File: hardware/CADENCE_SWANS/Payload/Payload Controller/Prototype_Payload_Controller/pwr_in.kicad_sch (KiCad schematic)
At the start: 0 parts

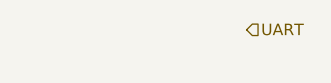
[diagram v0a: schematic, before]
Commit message: Instrument.sch updates
Added Control Readout module, and made it more legible and clean
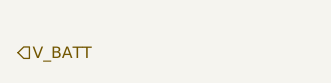
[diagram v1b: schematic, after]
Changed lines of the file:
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@@
 	(generator_version "9.0")
 	(paper "A5")
-	(hierarchical_label "UART"
+	(hierarchical_label "V_BATT"
 		(shape input)
-		(at 85.09 54.61 0)
+		(at 59.69 57.15 0)
 		(effects
 			(font

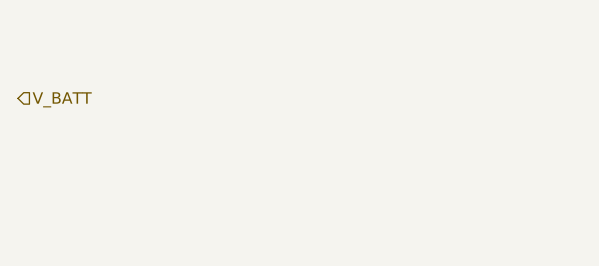
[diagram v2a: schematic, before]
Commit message: power management updates
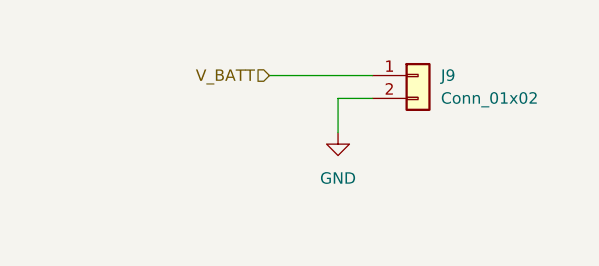
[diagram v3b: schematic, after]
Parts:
- added J9: Conn_01x02, symbol Connector_Generic:Conn_01x02
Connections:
- net V_BATT: now also J9.1 (Pin_1)
- new net GND: J9.2 (Pin_2)
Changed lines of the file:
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@@
 	(generator_version "9.0")
 	(paper "A5")
+	(wire
+		(pts
+			(xy 95.25 57.15) (xy 99.06 57.15)
+		)
+		(stroke
+			(width 0)
+			(type default)
+		)
+	)
+	(wire
+		(pts
+			(xy 95.25 60.96) (xy 95.25 57.15)
+		)
+		(stroke
+			(width 0)
+			(type default)
+		)
+	)
+	(wire
+		(pts
+			(xy 87.63 54.61) (xy 99.06 54.61)
+		)
+		(stroke
+			(width 0)
+			(type default)
+		)
+	)
 	(hierarchical_label "V_BATT"
 		(shape input)
-		(at 59.69 57.15 0)
+		(at 87.63 54.61 180)
 		(effects
 			(font
 				(size 1.27 1.27)
 			)
-			(justify left)
+			(justify right)
 		)
 	)
+	(symbol
+		(lib_id "power:GND")
+		(at 95.25 60.96 0)
+		(unit 1)
+		(exclude_from_sim no)
+		(in_bom yes)
+		(on_board yes)
+		(dnp no)
+		(fields_autoplaced yes)
+		(property "Reference" "#PWR024"
+			(at 95.25 67.31 0)
+			(effects
+				(font
+					(size 1.27 1.27)
+				)
+				(hide yes)
+			)
+		)
+		(property "Value" "GND"
+			(at 95.25 66.04 0)
+			(effects
+				(font
+					(size 1.27 1.27)
+				)
+			)
+		)
+		(property "Footprint" ""
+			(at 95.25 60.96 0)
+			(effects
+				(font
+					(size 1.27 1.27)
+				)
+				(hide yes)
+			)
+		)
+		(property "Datasheet" ""
+			(at 95.25 60.96 0)
+			(effects
+				(font
+					(size 1.27 1.27)
+				)
+				(hide yes)
+			)
+		)
+		(property "Description" "Power symbol creates a global label with name \"GND\" , ground"
+			(at 95.25 60.96 0)
+			(effects
+				(font
+					(size 1.27 1.27)
+				)
+				(hide yes)
+			)
+		)
+		(pin "1"
+		)
+		(instances
+			(project ""
+				(path "/866a965d-c307-40b7-9977-69e77fc0dc82/4cf906e6-065c-4b10-a5a2-987a95214f7a"
+					(reference "#PWR024")
+					(unit 1)
+				)
+			)
+		)
+	)
+	(symbol
+		(lib_id "Connector_Generic:Conn_01x02")
+		(at 104.14 54.61 0)
+		(unit 1)
+		(exclude_from_sim no)
+		(in_bom yes)
+		(on_board yes)
+		(dnp no)
+		(fields_autoplaced yes)
+		(property "Reference" "J9"
+			(at 106.68 54.6099 0)
+			(effects
+				(font
+					(size 1.27 1.27)
+				)
+				(justify left)
+			)
+		)
+		(property "Value" "Conn_01x02"
+			(at 106.68 57.1499 0)
+			(effects
+				(font
+					(size 1.27 1.27)
+				)
+				(justify left)
+			)
+		)
+		(property "Footprint" ""
+			(at 104.14 54.61 0)
+			(effects
+				(font
+					(size 1.27 1.27)
+				)
+				(hide yes)
+			)
+		)
+		(property "Datasheet" "~"
+			(at 104.14 54.61 0)
+			(effects
+				(font
+					(size 1.27 1.27)
+				)
+				(hide yes)
+			)
+		)
+		(property "Description" "Generic connector, single row, 01x02, script generated (kicad-library-utils/schlib/autogen/connector/)"
+			(at 104.14 54.61 0)
+			(effects
+				(font
+					(size 1.27 1.27)
+				)
+				(hide yes)
+			)
+		)
+		(pin "1"
+		)
+		(pin "2"
+		)
+		(instances
+			(project ""
+				(path "/866a965d-c307-40b7-9977-69e77fc0dc82/4cf906e6-065c-4b10-a5a2-987a95214f7a"
+					(reference "J9")
+					(unit 1)
+				)
+			)
+		)
+	)

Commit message: updates
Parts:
- J9: footprint (none) -> Connector_AMASS:AMASS_XT60-F_1x02_P7.20mm_Vertical
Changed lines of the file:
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@@
 	(generator_version "9.0")
 	(paper "A5")
+	(junction
+		(at 92.71 54.61)
+		(diameter 0)
+		(color 0 0 0 0)
+	)
+	(wire
+		(pts
+			(xy 92.71 54.61) (xy 99.06 54.61)
+		)
+		(stroke
+			(width 0)
+			(type default)
+		)
+	)
 	(wire
 		(pts
@@
 	(wire
 		(pts
-			(xy 87.63 54.61) (xy 99.06 54.61)
+			(xy 87.63 54.61) (xy 92.71 54.61)
 		)
 		(stroke
@@
 	)
 	(symbol
+		(lib_id "power:PWR_FLAG")
+		(at 92.71 54.61 0)
+		(unit 1)
+		(exclude_from_sim no)
+		(in_bom yes)
+		(on_board yes)
+		(dnp no)
+		(fields_autoplaced yes)
+		(property "Reference" "#FLG08"
+			(at 92.71 52.705 0)
+			(effects
+				(font
+					(size 1.27 1.27)
+				)
+				(hide yes)
+			)
+		)
+		(property "Value" "PWR_FLAG"
+			(at 92.71 49.53 0)
+			(effects
+				(font
+					(size 1.27 1.27)
+				)
+			)
+		)
+		(property "Footprint" ""
+			(at 92.71 54.61 0)
+			(effects
+				(font
+					(size 1.27 1.27)
+				)
+				(hide yes)
+			)
+		)
+		(property "Datasheet" "~"
+			(at 92.71 54.61 0)
+			(effects
+				(font
+					(size 1.27 1.27)
+				)
+				(hide yes)
+			)
+		)
+		(property "Description" "Special symbol for telling ERC where power comes from"
+			(at 92.71 54.61 0)
+			(effects
+				(font
+					(size 1.27 1.27)
+				)
+				(hide yes)
+			)
+		)
+		(pin "1"
+		)
+		(instances
+			(project "Payload_Controller_EM"
+				(path "/866a965d-c307-40b7-9977-69e77fc0dc82/4cf906e6-065c-4b10-a5a2-987a95214f7a"
+					(reference "#FLG08")
+					(unit 1)
+				)
+			)
+		)
+	)
+	(symbol
 		(lib_id "Connector_Generic:Conn_01x02")
 		(at 104.14 54.61 0)
@@
 			)
 		)
-		(property "Footprint" ""
+		(property "Footprint" "Connector_AMASS:AMASS_XT60-F_1x02_P7.20mm_Vertical"
 			(at 104.14 54.61 0)
 			(effects

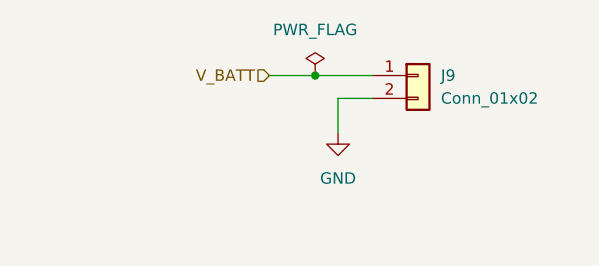
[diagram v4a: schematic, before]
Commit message: linked more footprints
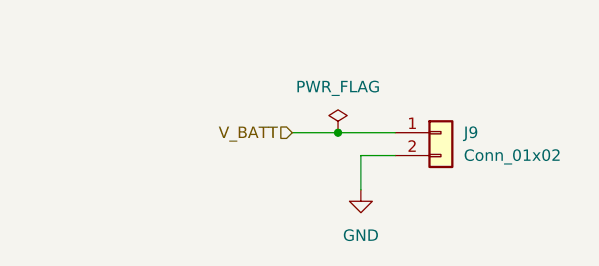
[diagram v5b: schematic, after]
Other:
- moved on the sheet: J9
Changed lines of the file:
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@@
 	(paper "A5")
 	(junction
-		(at 92.71 54.61)
+		(at 95.25 60.96)
 		(diameter 0)
 		(color 0 0 0 0)
@@
 	(wire
 		(pts
-			(xy 92.71 54.61) (xy 99.06 54.61)
-		)
-		(stroke
-			(width 0)
-			(type default)
-		)
-	)
-	(wire
-		(pts
-			(xy 95.25 57.15) (xy 99.06 57.15)
-		)
-		(stroke
-			(width 0)
-			(type default)
-		)
-	)
-	(wire
-		(pts
-			(xy 95.25 60.96) (xy 95.25 57.15)
-		)
-		(stroke
-			(width 0)
-			(type default)
-		)
-	)
-	(wire
-		(pts
-			(xy 87.63 54.61) (xy 92.71 54.61)
+			(xy 95.25 60.96) (xy 101.6 60.96)
+		)
+		(stroke
+			(width 0)
+			(type default)
+		)
+	)
+	(wire
+		(pts
+			(xy 97.79 63.5) (xy 101.6 63.5)
+		)
+		(stroke
+			(width 0)
+			(type default)
+		)
+	)
+	(wire
+		(pts
+			(xy 97.79 67.31) (xy 97.79 63.5)
+		)
+		(stroke
+			(width 0)
+			(type default)
+		)
+	)
+	(wire
+		(pts
+			(xy 90.17 60.96) (xy 95.25 60.96)
 		)
 		(stroke
@@
 	(hierarchical_label "V_BATT"
 		(shape input)
-		(at 87.63 54.61 180)
+		(at 90.17 60.96 180)
 		(effects
 			(font
@@
 	(symbol
 		(lib_id "power:GND")
+		(at 97.79 67.31 0)
+		(unit 1)
+		(exclude_from_sim no)
+		(in_bom yes)
+		(on_board yes)
+		(dnp no)
+		(fields_autoplaced yes)
+		(property "Reference" "#PWR024"
+			(at 97.79 73.66 0)
+			(effects
+				(font
+					(size 1.27 1.27)
+				)
+				(hide yes)
+			)
+		)
+		(property "Value" "GND"
+			(at 97.79 72.39 0)
+			(effects
+				(font
+					(size 1.27 1.27)
+				)
+			)
+		)
+		(property "Footprint" ""
+			(at 97.79 67.31 0)
+			(effects
+				(font
+					(size 1.27 1.27)
+				)
+				(hide yes)
+			)
+		)
+		(property "Datasheet" ""
+			(at 97.79 67.31 0)
+			(effects
+				(font
+					(size 1.27 1.27)
+				)
+				(hide yes)
+			)
+		)
+		(property "Description" "Power symbol creates a global label with name \"GND\" , ground"
+			(at 97.79 67.31 0)
+			(effects
+				(font
+					(size 1.27 1.27)
+				)
+				(hide yes)
+			)
+		)
+		(pin "1"
+		)
+		(instances
+			(project ""
+				(path "/866a965d-c307-40b7-9977-69e77fc0dc82/4cf906e6-065c-4b10-a5a2-987a95214f7a"
+					(reference "#PWR024")
+					(unit 1)
+				)
+			)
+		)
+	)
+	(symbol
+		(lib_id "power:PWR_FLAG")
 		(at 95.25 60.96 0)
 		(unit 1)
@@
 		(dnp no)
 		(fields_autoplaced yes)
-		(property "Reference" "#PWR024"
-			(at 95.25 67.31 0)
-			(effects
-				(font
-					(size 1.27 1.27)
-				)
-				(hide yes)
-			)
-		)
-		(property "Value" "GND"
-			(at 95.25 66.04 0)
+		(property "Reference" "#FLG08"
+			(at 95.25 59.055 0)
+			(effects
+				(font
+					(size 1.27 1.27)
+				)
+				(hide yes)
+			)
+		)
+		(property "Value" "PWR_FLAG"
+			(at 95.25 55.88 0)
 			(effects
 				(font
@@
 			)
 		)
-		(property "Datasheet" ""
+		(property "Datasheet" "~"
 			(at 95.25 60.96 0)
 			(effects
@@
 			)
 		)
-		(property "Description" "Power symbol creates a global label with name \"GND\" , ground"
+		(property "Description" "Special symbol for telling ERC where power comes from"
 			(at 95.25 60.96 0)
-			(effects
-				(font
-					(size 1.27 1.27)
-				)
-				(hide yes)
-			)
-		)
-		(pin "1"
-		)
-		(instances
-			(project ""
-				(path "/866a965d-c307-40b7-9977-69e77fc0dc82/4cf906e6-065c-4b10-a5a2-987a95214f7a"
-					(reference "#PWR024")
-					(unit 1)
-				)
-			)
-		)
-	)
-	(symbol
-		(lib_id "power:PWR_FLAG")
-		(at 92.71 54.61 0)
-		(unit 1)
-		(exclude_from_sim no)
-		(in_bom yes)
-		(on_board yes)
-		(dnp no)
-		(fields_autoplaced yes)
-		(property "Reference" "#FLG08"
-			(at 92.71 52.705 0)
-			(effects
-				(font
-					(size 1.27 1.27)
-				)
-				(hide yes)
-			)
-		)
-		(property "Value" "PWR_FLAG"
-			(at 92.71 49.53 0)
-			(effects
-				(font
-					(size 1.27 1.27)
-				)
-			)
-		)
-		(property "Footprint" ""
-			(at 92.71 54.61 0)
-			(effects
-				(font
-					(size 1.27 1.27)
-				)
-				(hide yes)
-			)
-		)
-		(property "Datasheet" "~"
-			(at 92.71 54.61 0)
-			(effects
-				(font
-					(size 1.27 1.27)
-				)
-				(hide yes)
-			)
-		)
-		(property "Description" "Special symbol for telling ERC where power comes from"
-			(at 92.71 54.61 0)
 			(effects
 				(font
@@
 	(symbol
 		(lib_id "Connector_Generic:Conn_01x02")
-		(at 104.14 54.61 0)
+		(at 106.68 60.96 0)
 		(unit 1)
 		(exclude_from_sim no)
@@
 		(fields_autoplaced yes)
 		(property "Reference" "J9"
-			(at 106.68 54.6099 0)
+			(at 109.22 60.9599 0)
 			(effects
 				(font
@@
 		)
 		(property "Value" "Conn_01x02"
-			(at 106.68 57.1499 0)
+			(at 109.22 63.4999 0)
 			(effects
 				(font
@@
 		)
 		(property "Footprint" "Connector_AMASS:AMASS_XT60-F_1x02_P7.20mm_Vertical"
-			(at 104.14 54.61 0)
+			(at 106.68 60.96 0)
 			(effects
 				(font
@@
 		)
 		(property "Datasheet" "~"
-			(at 104.14 54.61 0)
+			(at 106.68 60.96 0)
 			(effects
 				(font
@@
 		)
 		(property "Description" "Generic connector, single row, 01x02, script generated (kicad-library-utils/schlib/autogen/connector/)"
-			(at 104.14 54.61 0)
-			(effects
-				(font
+			(at 106.68 60.96 0)
+			(effects
+				(font

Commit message: updates
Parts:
- renumbered J9 to J14
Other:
- moved on the sheet: J14
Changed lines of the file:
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@@
 	(paper "A5")
 	(junction
-		(at 95.25 60.96)
+		(at 91.44 57.15)
 		(diameter 0)
 		(color 0 0 0 0)
@@
 	(wire
 		(pts
-			(xy 95.25 60.96) (xy 101.6 60.96)
-		)
-		(stroke
-			(width 0)
-			(type default)
-		)
-	)
-	(wire
-		(pts
-			(xy 97.79 63.5) (xy 101.6 63.5)
-		)
-		(stroke
-			(width 0)
-			(type default)
-		)
-	)
-	(wire
-		(pts
-			(xy 97.79 67.31) (xy 97.79 63.5)
-		)
-		(stroke
-			(width 0)
-			(type default)
-		)
-	)
-	(wire
-		(pts
-			(xy 90.17 60.96) (xy 95.25 60.96)
+			(xy 91.44 57.15) (xy 85.09 57.15)
+		)
+		(stroke
+			(width 0)
+			(type default)
+		)
+	)
+	(wire
+		(pts
+			(xy 88.9 59.69) (xy 85.09 59.69)
+		)
+		(stroke
+			(width 0)
+			(type default)
+		)
+	)
+	(wire
+		(pts
+			(xy 88.9 63.5) (xy 88.9 59.69)
+		)
+		(stroke
+			(width 0)
+			(type default)
+		)
+	)
+	(wire
+		(pts
+			(xy 96.52 57.15) (xy 91.44 57.15)
 		)
 		(stroke
@@
 	(hierarchical_label "V_BATT"
 		(shape input)
-		(at 90.17 60.96 180)
+		(at 96.52 57.15 0)
 		(effects
 			(font
 				(size 1.27 1.27)
 			)
-			(justify right)
+			(justify left)
 		)
 	)
 	(symbol
 		(lib_id "power:GND")
-		(at 97.79 67.31 0)
+		(at 88.9 63.5 0)
+		(mirror y)
 		(unit 1)
 		(exclude_from_sim no)
@@
 		(dnp no)
 		(fields_autoplaced yes)
-		(property "Reference" "#PWR024"
-			(at 97.79 73.66 0)
+		(property "Reference" "#PWR0102"
+			(at 88.9 69.85 0)
 			(effects
 				(font
@@
 		)
 		(property "Value" "GND"
-			(at 97.79 72.39 0)
+			(at 88.9 68.58 0)
 			(effects
 				(font
@@
 		)
 		(property "Footprint" ""
-			(at 97.79 67.31 0)
+			(at 88.9 63.5 0)
 			(effects
 				(font
@@
 		)
 		(property "Datasheet" ""
-			(at 97.79 67.31 0)
+			(at 88.9 63.5 0)
 			(effects
 				(font
@@
 		)
 		(property "Description" "Power symbol creates a global label with name \"GND\" , ground"
-			(at 97.79 67.31 0)
+			(at 88.9 63.5 0)
 			(effects
 				(font
@@
 			(project ""
 				(path "/866a965d-c307-40b7-9977-69e77fc0dc82/4cf906e6-065c-4b10-a5a2-987a95214f7a"
-					(reference "#PWR024")
+					(reference "#PWR0102")
 					(unit 1)
 				)
@@
 	(symbol
 		(lib_id "power:PWR_FLAG")
-		(at 95.25 60.96 0)
+		(at 91.44 57.15 0)
+		(mirror y)
 		(unit 1)
 		(exclude_from_sim no)
@@
 		(dnp no)
 		(fields_autoplaced yes)
-		(property "Reference" "#FLG08"
-			(at 95.25 59.055 0)
+		(property "Reference" "#FLG03"
+			(at 91.44 55.245 0)
 			(effects
 				(font
@@
 		)
 		(property "Value" "PWR_FLAG"
-			(at 95.25 55.88 0)
+			(at 91.44 52.07 0)
 			(effects
 				(font
@@
 		)
 		(property "Footprint" ""
-			(at 95.25 60.96 0)
+			(at 91.44 57.15 0)
 			(effects
 				(font
@@
 		)
 		(property "Datasheet" "~"
-			(at 95.25 60.96 0)
+			(at 91.44 57.15 0)
 			(effects
 				(font
@@
 		)
 		(property "Description" "Special symbol for telling ERC where power comes from"
-			(at 95.25 60.96 0)
+			(at 91.44 57.15 0)
 			(effects
 				(font
@@
 			(project "Payload_Controller_EM"
 				(path "/866a965d-c307-40b7-9977-69e77fc0dc82/4cf906e6-065c-4b10-a5a2-987a95214f7a"
-					(reference "#FLG08")
+					(reference "#FLG03")
 					(unit 1)
 				)
@@
 	(symbol
 		(lib_id "Connector_Generic:Conn_01x02")
-		(at 106.68 60.96 0)
+		(at 80.01 57.15 0)
+		(mirror y)
 		(unit 1)
 		(exclude_from_sim no)
@@
 		(dnp no)
 		(fields_autoplaced yes)
-		(property "Reference" "J9"
-			(at 109.22 60.9599 0)
+		(property "Reference" "J14"
+			(at 77.47 57.1499 0)
 			(effects
 				(font
@@
 		)
 		(property "Value" "Conn_01x02"
-			(at 109.22 63.4999 0)
+			(at 77.47 59.6899 0)
 			(effects
 				(font
@@
 		)
 		(property "Footprint" "Connector_AMASS:AMASS_XT60-F_1x02_P7.20mm_Vertical"
-			(at 106.68 60.96 0)
+			(at 80.01 57.15 0)
 			(effects
 				(font
@@
 		)
 		(property "Datasheet" "~"
-			(at 106.68 60.96 0)
+			(at 80.01 57.15 0)
 			(effects
 				(font
@@
 		)
 		(property "Description" "Generic connector, single row, 01x02, script generated (kicad-library-utils/schlib/autogen/connector/)"
-			(at 106.68 60.96 0)
+			(at 80.01 57.15 0)
 			(effects
 				(font
@@
 			(project ""
 				(path "/866a965d-c307-40b7-9977-69e77fc0dc82/4cf906e6-065c-4b10-a5a2-987a95214f7a"
-					(reference "J9")
+					(reference "J14")
 					(unit 1)
 				)
